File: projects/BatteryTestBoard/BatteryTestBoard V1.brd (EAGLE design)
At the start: 188.8 x 115.2 mm, 142 parts, among them M2 IPB120P04P4L03ATMA1, SW1 BTS50015-1TAD, U1 LTC4121-4.2, U2 AD8418, U3 AD8418, U4 LC05111C13MTTTG, U5 LTC4121, U6 AP9211SA-AG-HAC-7, U7 VNS3NV04DP-E

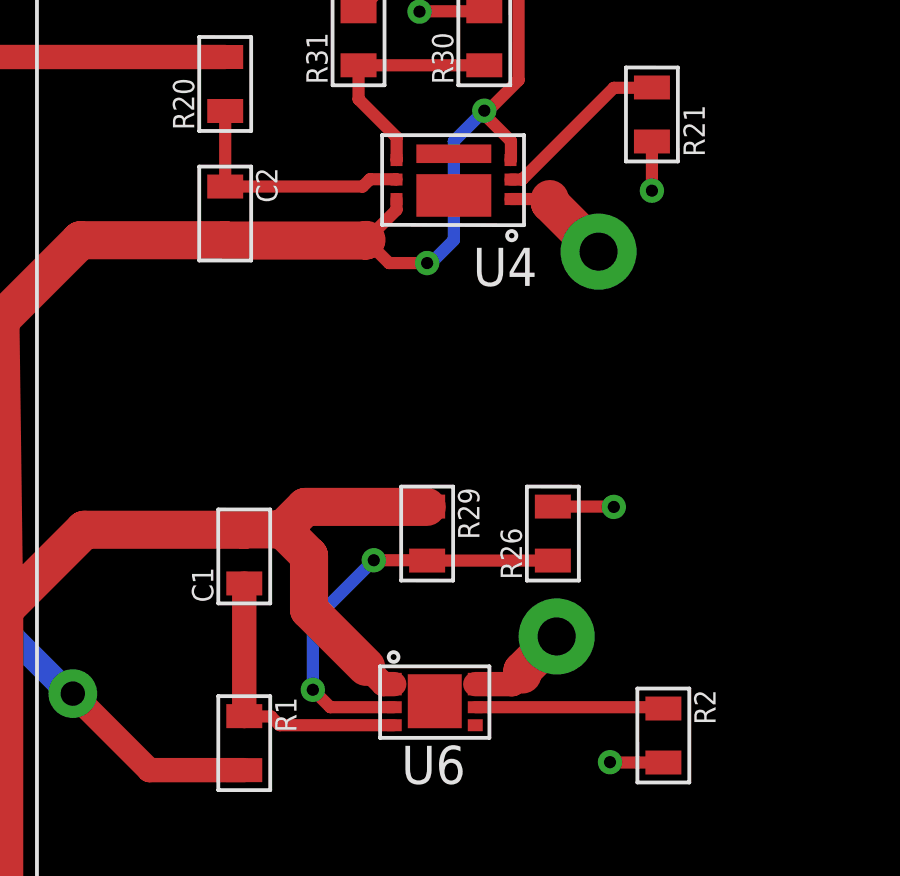
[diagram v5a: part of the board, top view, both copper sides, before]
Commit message: Fixing FreeDFM clearance issues with AP9211
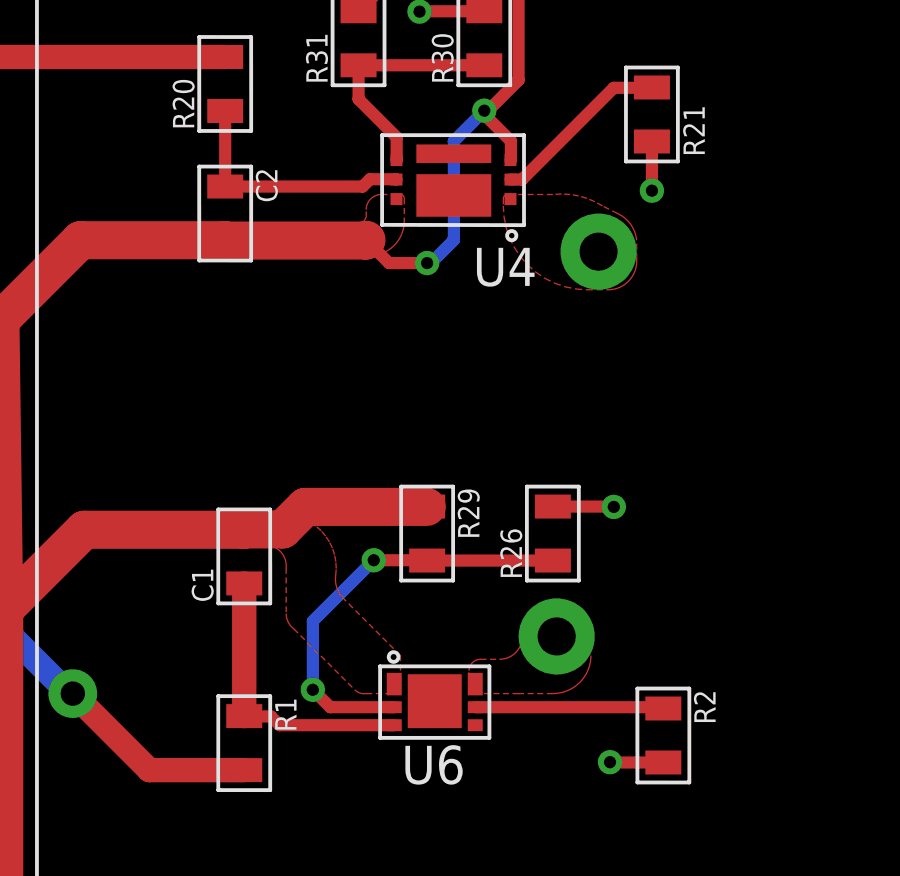
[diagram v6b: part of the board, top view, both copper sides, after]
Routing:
- net N$9: track 141.4 -> 132.8 mm
- net GND: track 137.8 -> 130.6 mm
- added copper zone on layer 1, net N$9
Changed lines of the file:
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@@
 <wire x1="44.958" y1="83.936" x2="44.958" y2="82.423" width="0.4064" layer="1"/>
 <via x="44.958" y="82.423" extent="1-16" drill="0.4064" diameter="0.8128"/>
-<wire x1="64.262" y1="45.266" x2="64.254" y2="45.274" width="0.4064" layer="1"/>
 <wire x1="69.342" y1="42.661" x2="67.575" y2="42.661" width="0.4064" layer="1"/>
 <wire x1="67.575" y1="42.661" x2="67.564" y2="42.672" width="0.4064" layer="1"/>
@@
 <wire x1="68.961" y1="63.362" x2="68.961" y2="61.722" width="0.4064" layer="1"/>
 <via x="68.961" y="61.722" extent="1-16" drill="0.4064" diameter="0.8128"/>
-<wire x1="64.247" y1="61.443" x2="65.557" y2="61.443" width="0.4064" layer="1"/>
 <contactref element="R26" pad="2"/>
 <contactref element="R30" pad="2"/>
@@
 <wire x1="104.648" y1="46.863" x2="104.648" y2="62.044" width="0.8128" layer="1"/>
 <wire x1="104.648" y1="62.044" x2="103.378" y2="63.314" width="0.8128" layer="1"/>
-<wire x1="63.072" y1="45.274" x2="64.254" y2="45.274" width="0.8128" layer="1"/>
-<wire x1="64.254" y1="45.274" x2="64.324" y2="45.274" width="0.8128" layer="1"/>
-<wire x1="64.324" y1="45.274" x2="64.643" y2="45.593" width="0.8128" layer="1"/>
-<wire x1="64.643" y1="45.593" x2="64.643" y2="45.72" width="1.27" layer="1"/>
-<wire x1="64.643" y1="45.72" x2="65.786" y2="46.863" width="1.27" layer="1"/>
 <via x="65.786" y="46.863" extent="1-16" drill="1.27" diameter="2.54"/>
-<wire x1="65.557" y1="61.443" x2="65.557" y2="61.316" width="1.27" layer="1"/>
-<wire x1="65.557" y1="61.316" x2="67.183" y2="59.69" width="1.27" layer="1"/>
 <via x="67.183" y="59.69" extent="1-16" drill="1.27" diameter="2.54"/>
 <wire x1="67.183" y1="59.69" x2="67.183" y2="59.817" width="1.27" layer="16"/>
@@
 <via x="93.472" y="39.751" extent="1-16" drill="0.4064" diameter="0.8128"/>
 <wire x1="93.995" y1="39.228" x2="93.472" y2="39.751" width="0.4064" layer="1"/>
+<polygon width="0.1524" layer="1" thermals="no">
+<vertex x="64.516" y="44.958"/>
+<vertex x="62.992" y="44.958" curve="-90"/>
+<vertex x="62.865" y="45.085"/>
+<vertex x="62.865" y="45.466"/>
+<vertex x="62.865" y="45.72" curve="-90"/>
+<vertex x="63.246" y="46.101"/>
+<vertex x="63.881" y="46.101" curve="90"/>
+<vertex x="64.643" y="46.863" curve="-90"/>
+<vertex x="65.786" y="48.006"/>
+<vertex x="65.913" y="48.006" curve="-90"/>
+<vertex x="66.929" y="46.99"/>
+<vertex x="66.929" y="46.863"/>
+<vertex x="66.929" y="46.228" curve="-90"/>
+<vertex x="65.659" y="44.958"/>
+</polygon>
+<polygon width="0.1524" layer="1" thermals="no">
+<vertex x="67.564" y="58.42" curve="90"/>
+<vertex x="68.453" y="59.436"/>
+<vertex x="68.453" y="60.071" curve="59.489763"/>
+<vertex x="67.818" y="60.96"/>
+<vertex x="67.31" y="61.214" curve="39.534385"/>
+<vertex x="65.659" y="61.595"/>
+<vertex x="64.135" y="61.595" curve="90"/>
+<vertex x="64.008" y="61.468"/>
+<vertex x="64.008" y="61.214" curve="90"/>
+<vertex x="66.802" y="58.42"/>
+</polygon>
 </signal>
 <signal name="!LIONFAULT">
@@
 <contactref element="R24" pad="P$2"/>
 <wire x1="12.573" y1="30.412" x2="18.923" y2="30.412" width="0.8128" layer="1"/>
-<wire x1="60.372" y1="45.212859375" x2="60.372" y2="45.274" width="0.4064" layer="1"/>
-<wire x1="60.371140625" y1="45.212" x2="60.372" y2="45.212859375" width="0.4064" layer="1"/>
 <contactref element="R29" pad="1"/>
 <contactref element="R31" pad="2"/>
@@
 <wire x1="60.314" y1="68.834" x2="59.182" y2="67.702" width="0.4064" layer="1"/>
 <wire x1="59.447" y1="60.082" x2="59.447" y2="60.06" width="0.4064" layer="1"/>
-<wire x1="60.447" y1="61.443" x2="60.447" y2="61.082" width="0.4064" layer="1"/>
-<wire x1="60.447" y1="61.082" x2="59.447" y2="60.082" width="0.4064" layer="1"/>
 <wire x1="50.038" y1="50.419" x2="47.371" y2="47.752" width="1.27" layer="1"/>
 <wire x1="50.038" y1="50.419" x2="55.361" y2="50.419" width="1.27" layer="1"/>
@@
 <wire x1="57.404" y1="51.181" x2="61.457" y2="51.181" width="1.27" layer="1"/>
 <wire x1="56.769" y1="50.314" x2="56.653" y2="50.43" width="0.8128" layer="1"/>
-<wire x1="60.372" y1="45.274" x2="60.009" y2="45.274" width="0.8128" layer="1"/>
-<wire x1="60.009" y1="45.274" x2="59.436" y2="45.847" width="0.8128" layer="1"/>
-<wire x1="59.436" y1="45.847" x2="57.531" y2="47.752" width="1.27" layer="1"/>
-<wire x1="57.531" y1="47.752" x2="57.531" y2="49.552" width="1.27" layer="1"/>
-<wire x1="57.531" y1="49.552" x2="56.769" y2="50.314" width="1.27" layer="1"/>
 <wire x1="54.737" y1="60.06" x2="59.425" y2="60.06" width="1.27" layer="1"/>
 <wire x1="59.425" y1="60.06" x2="59.447" y2="60.082" width="1.27" layer="1"/>
+<polygon width="0.1524" layer="1" thermals="no">
+<vertex x="56.007" y="49.911"/>
+<vertex x="56.134" y="49.911" curve="-90"/>
+<vertex x="56.769" y="49.149"/>
+<vertex x="56.769" y="47.625" curve="53.130102"/>
+<vertex x="57.023" y="47.117"/>
+<vertex x="59.055" y="45.085" curve="53.130102"/>
+<vertex x="59.436" y="44.958"/>
+<vertex x="60.452" y="44.958" curve="90"/>
+<vertex x="60.579" y="45.085"/>
+<vertex x="60.579" y="46.228"/>
+<vertex x="58.674" y="48.133" curve="-53.130102"/>
+<vertex x="58.42" y="48.895" curve="119.679415"/>
+<vertex x="56.007" y="50.8"/>
+</polygon>
+<polygon width="0.1524" layer="1" thermals="no">
+<vertex x="58.547" y="60.579"/>
+<vertex x="58.801" y="60.579" curve="90"/>
+<vertex x="59.436" y="60.833"/>
+<vertex x="59.436" y="61.087" curve="-90"/>
+<vertex x="59.944" y="61.595"/>
+<vertex x="60.579" y="61.595" curve="-90"/>
+<vertex x="60.706" y="61.468"/>
+<vertex x="60.706" y="60.706" curve="-90"/>
+<vertex x="59.563" y="59.563" curve="-90"/>
+</polygon>
 </signal>
 <signal name="N$4">
